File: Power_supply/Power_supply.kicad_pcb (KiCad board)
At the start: 2 copper layers, 115 x 50 mm, 19 parts, among them X1 DG301-5.0-02P, X2 DG301-5.0-03P

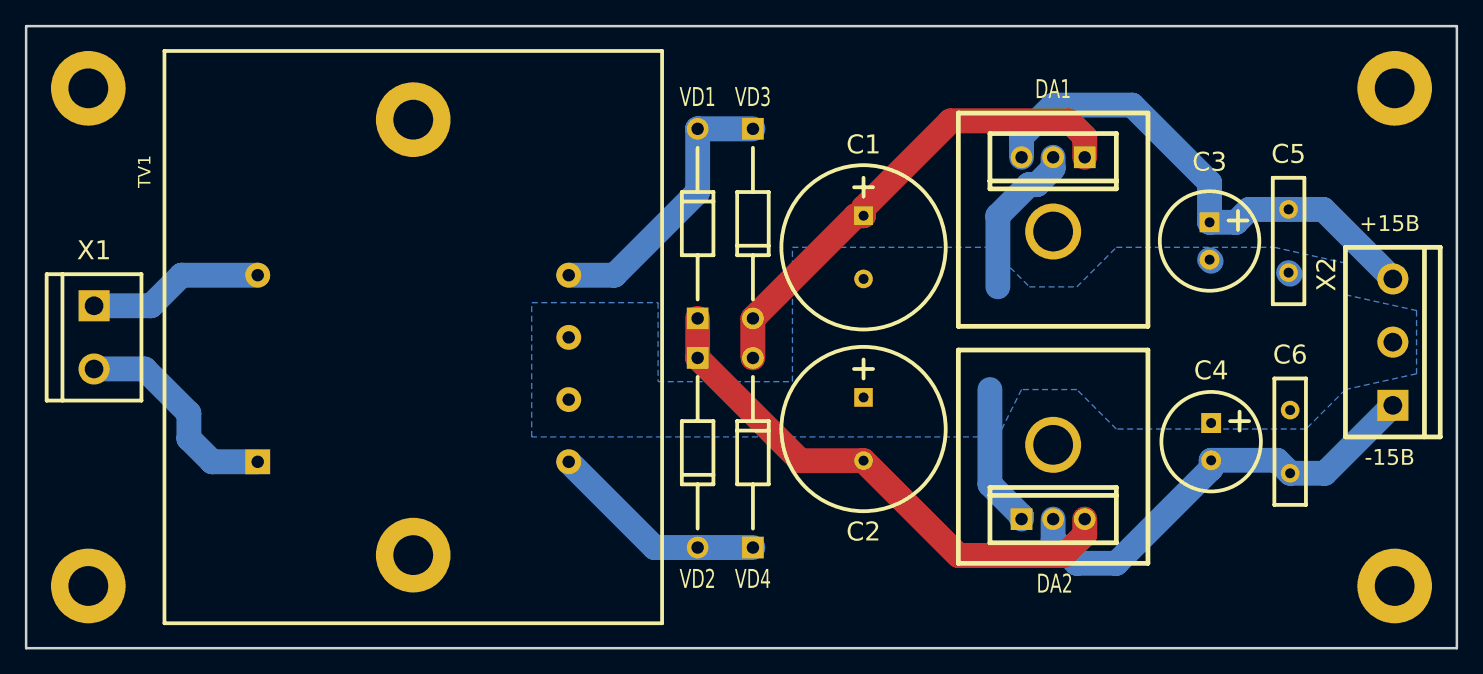
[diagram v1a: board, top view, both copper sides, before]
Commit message: Поправил ошибки в схеме и на печатной плате Power_supply.
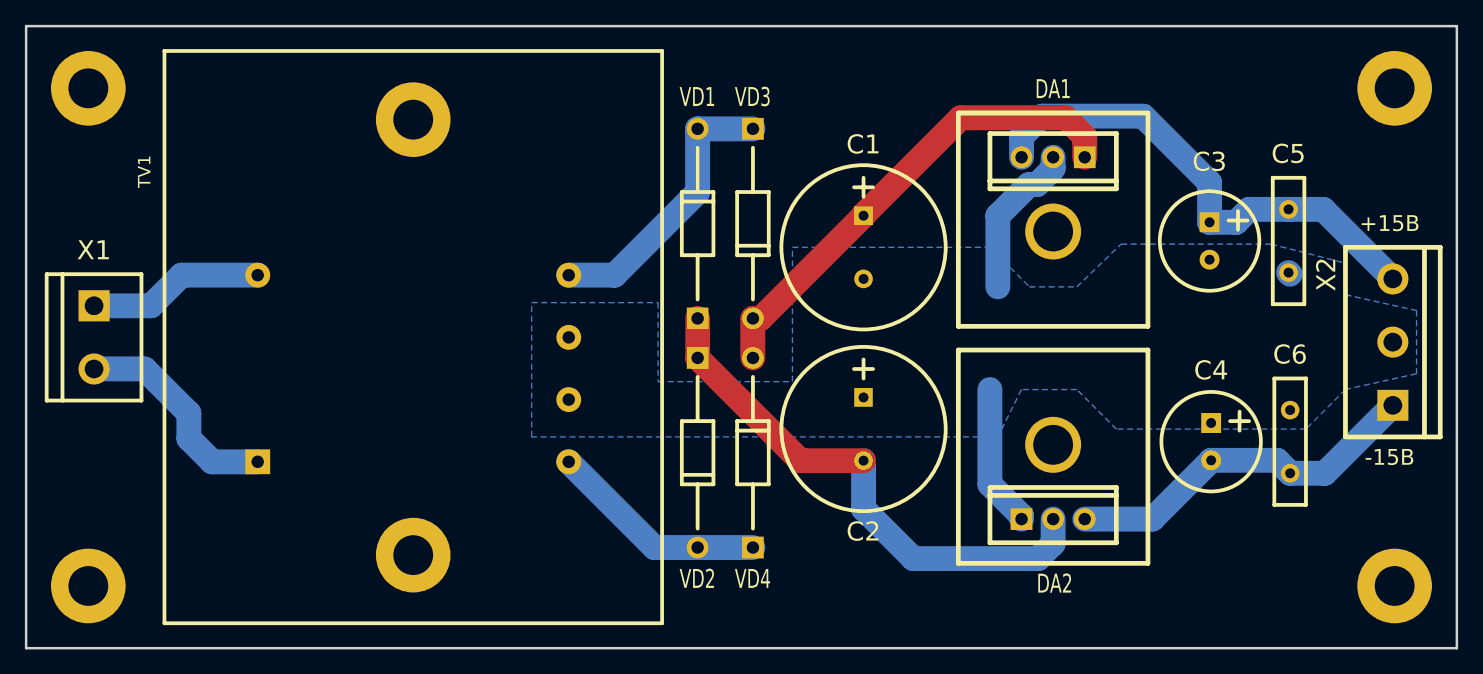
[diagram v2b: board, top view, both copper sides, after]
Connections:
- DA2 pad 2: /-15V -> Net-(C2-Pad2)
- DA2 pad 3: Net-(C2-Pad2) -> /-15V
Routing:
- net /-15V: track 36.3 -> 29.4 mm
- net /+15V: track 41.1 -> 40.3 mm
